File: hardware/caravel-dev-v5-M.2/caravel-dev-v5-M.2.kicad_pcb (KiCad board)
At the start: 2 copper layers, 76.2 x 73.8 mm, 64 parts, among them J1 USB_B_Micro - 10118193-0001LF, J10 Conn_01x27_Female, J11 Conn_01x20_Female, J2 Conn_01x02_Female, J3 Conn_01x02_Male, J4 Conn_01x04_Female, J5 Conn_01x02_Male, J6 Conn_01x02_Male, J7 Conn_01x06_Female, J8 Conn_01x02_Male, J9 Conn_01x02_Male, SW1 SW_Push - SKQGADE010, T1 Logo, T2 Logo, U1 FT232H, U2 SN74LVC1G125DCKR, U3 SN74LVC1G125DCKR, U4 MCP1319MT-29LE-OT, U5 TAR5SxxU_SOT353F, U6 TAR5SxxU_SOT353F, U7 W25Q32FVSS, U8 caravel-M.2-card, X1 DSC6001_10MHZ, Y1 CSTNE12M0GH5L000R0

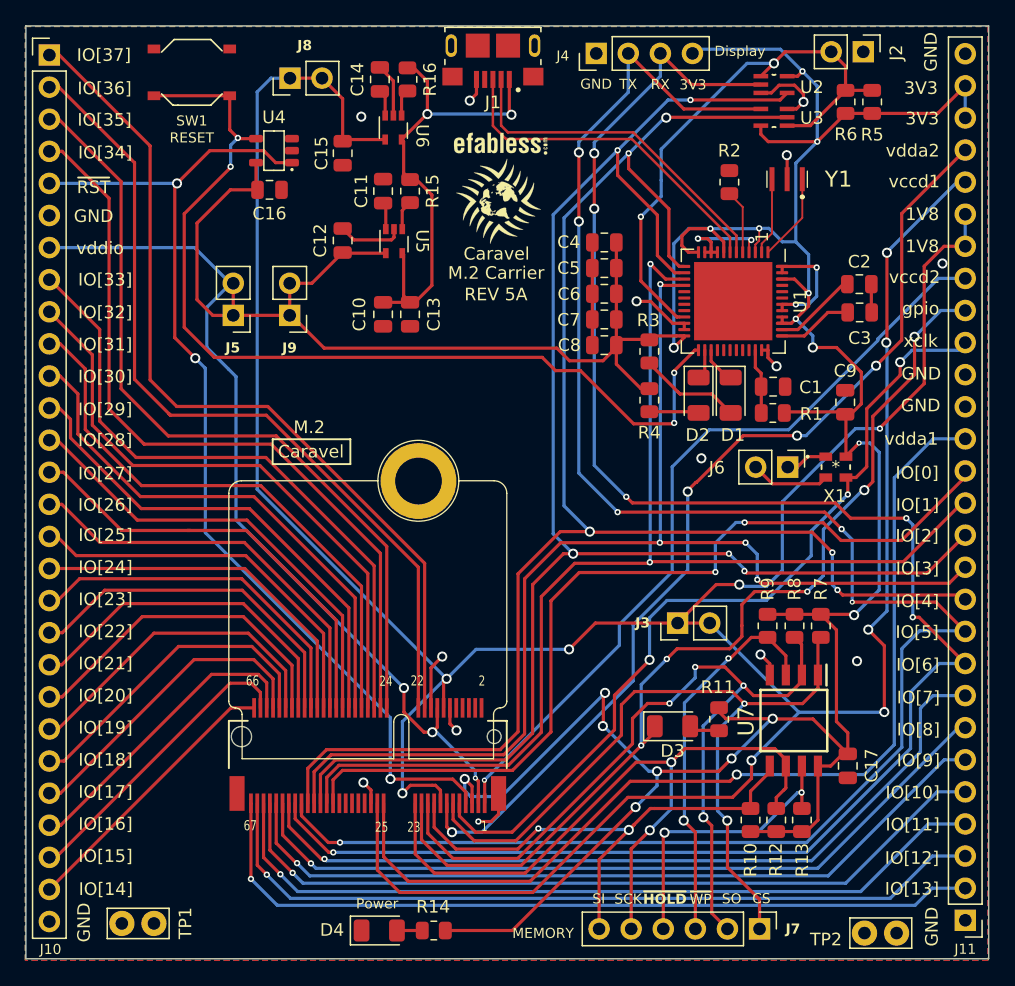
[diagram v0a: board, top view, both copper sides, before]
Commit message: rename caravel M.2 carrier board to caravel dev v5 board update Caravel dev (REV5A) pcb:   ~ update the serial display connector to 3-pin   + add large via for the manual reset to be able to monitor it
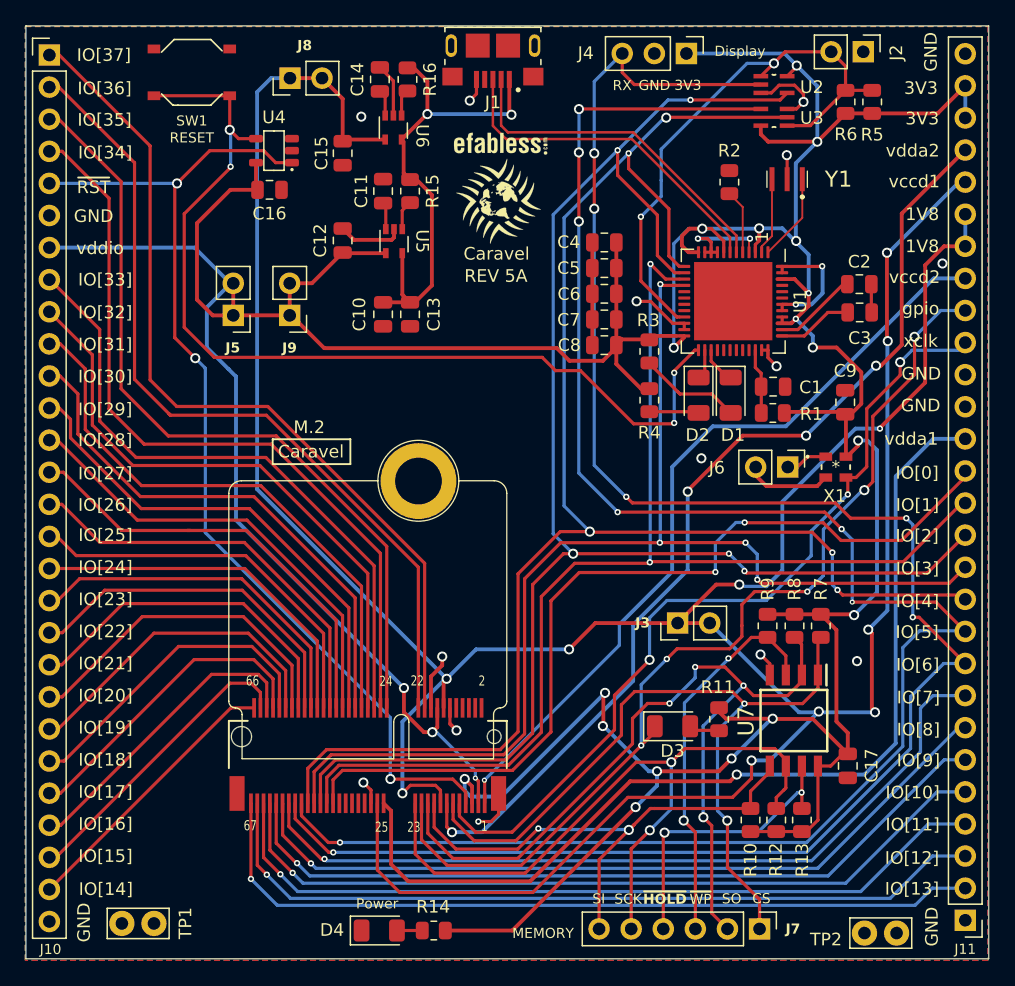
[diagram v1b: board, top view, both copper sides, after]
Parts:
- J4: value Conn_01x04_Female -> Conn_01x03_Female; footprint Connector_PinHeader_2.54mm:PinHeader_1x04_P2.54mm_Vertical -> Connector_PinHeader_2.54mm:PinHeader_1x03_P2.54mm_Vertical
- moved J4 7.14 mm to (147.3, 119.9), turned to -90 degrees
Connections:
- J4 pad 1: GND -> vdda
- J4 pad 2: mprj_io[5]_ser_rx -> GND
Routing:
- net mprj_io[5]_ser_rx: track 151.8 -> 147.8 mm, vias 6 -> 7
- net mprj_io[6]_ser_tx: track 148.1 -> 150.5 mm
- net GND: track 74.7 -> 75.9 mm
- net vdda: track 378.5 -> 379.4 mm, vias 20 -> 21
- net +5V: track 38.4 -> 39.1 mm
- net vccd: track 263.2 -> 263.7 mm, vias 10 -> 11
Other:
- board text removed: "M.2 Carrier"
- board text removed: "TX"

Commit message: add gerber files for Caravel dev (REV5A) and M.2 card pcbs
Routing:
- net mprj_io[33]: track 50.6 -> 49.7 mm
- net mprj_io[34]: track 61.4 -> 60.5 mm
- net mprj_io[32]: track 47.7 -> 46.9 mm
- net vdda: track 379.4 -> 379.7 mm, vias 21 -> 20
- net vccd: vias 11 -> 10
